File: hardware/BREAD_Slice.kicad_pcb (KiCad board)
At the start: 2 copper layers, 70 x 100 mm, 16 parts, among them J1 Conn_01x10_Female, U1 AP63205

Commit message: initial commit, complete schematic and board
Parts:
- added C10: 0.1u, Capacitor_SMD:C_0805_2012Metric_Pad1.18x1.45mm_HandSolder, F.Cu at (172.6, 102.2)
- added C11: 0.1u, Capacitor_SMD:C_0805_2012Metric_Pad1.18x1.45mm_HandSolder, F.Cu at (170.4, 65.9)
- added C12: 0.1u, Capacitor_SMD:C_0805_2012Metric_Pad1.18x1.45mm_HandSolder, F.Cu at (172.5, 65.9)
- added C5: 0.1u, Capacitor_SMD:C_0805_2012Metric_Pad1.18x1.45mm_HandSolder, F.Cu at (170.4, 120.5)
- added C6: 0.1u, Capacitor_SMD:C_0805_2012Metric_Pad1.18x1.45mm_HandSolder, F.Cu at (172.6, 120.5)
- added C7: 0.1u, Capacitor_SMD:C_0805_2012Metric_Pad1.18x1.45mm_HandSolder, F.Cu at (170.5, 84.1)
- added C8: 0.1u, Capacitor_SMD:C_0805_2012Metric_Pad1.18x1.45mm_HandSolder, F.Cu at (172.6, 84.1)
- added C9: 0.1u, Capacitor_SMD:C_0805_2012Metric_Pad1.18x1.45mm_HandSolder, F.Cu at (170.4, 102.2)
- added Cl1: 100n, Capacitor_SMD:C_0805_2012Metric_Pad1.18x1.45mm_HandSolder, F.Cu at (179.8, 112.9)
- added Cl2: 100n, Capacitor_SMD:C_0805_2012Metric_Pad1.18x1.45mm_HandSolder, F.Cu at (179.8, 76.5)
- added Cl3: 100n, Capacitor_SMD:C_0805_2012Metric_Pad1.18x1.45mm_HandSolder, F.Cu at (179.8, 94.5)
- added Cl4: 100n, Capacitor_SMD:C_0805_2012Metric_Pad1.18x1.45mm_HandSolder, F.Cu at (179.7, 58.3)
- added FB1: FerriteBead, Resistor_SMD:R_0805_2012Metric_Pad1.20x1.40mm_HandSolder, F.Cu at (174.6, 120.5)
- added FB2: FerriteBead, Resistor_SMD:R_0805_2012Metric_Pad1.20x1.40mm_HandSolder, F.Cu at (174.7, 84.1)
- added FB3: FerriteBead, Resistor_SMD:R_0805_2012Metric_Pad1.20x1.40mm_HandSolder, F.Cu at (174.7, 102.2)
- added FB4: FerriteBead, Resistor_SMD:R_0805_2012Metric_Pad1.20x1.40mm_HandSolder, F.Cu at (174.6, 65.9)
- added J2: Screw_Terminal_01x02, TerminalBlock_4Ucon:TerminalBlock_4Ucon_1x02_P3.50mm_Horizontal, F.Cu at (187.7, 118.0)
- added J3: Screw_Terminal_01x02, TerminalBlock_4Ucon:TerminalBlock_4Ucon_1x02_P3.50mm_Horizontal, F.Cu at (187.7, 109.0)
- added J4: Screw_Terminal_01x02, TerminalBlock_4Ucon:TerminalBlock_4Ucon_1x02_P3.50mm_Horizontal, F.Cu at (187.7, 99.7)
- added J5: Screw_Terminal_01x02, TerminalBlock_4Ucon:TerminalBlock_4Ucon_1x02_P3.50mm_Horizontal, F.Cu at (187.7, 90.6)
- added J6: Screw_Terminal_01x02, TerminalBlock_4Ucon:TerminalBlock_4Ucon_1x02_P3.50mm_Horizontal, F.Cu at (187.8, 81.5)
- added J7: Screw_Terminal_01x02, TerminalBlock_4Ucon:TerminalBlock_4Ucon_1x02_P3.50mm_Horizontal, F.Cu at (187.7, 72.5)
- added J8: Screw_Terminal_01x02, TerminalBlock_4Ucon:TerminalBlock_4Ucon_1x02_P3.50mm_Horizontal, F.Cu at (187.7, 63.4)
- added J9: Screw_Terminal_01x02, TerminalBlock_4Ucon:TerminalBlock_4Ucon_1x02_P3.50mm_Horizontal, F.Cu at (187.7, 54.3)
- added JP1: JUMP1, Jumper:SolderJumper-2_P1.3mm_Open_TrianglePad1.0x1.5mm, F.Cu at (179.4, 120.3)
- added JP10: JUMP2, Jumper:SolderJumper-2_P1.3mm_Bridged_RoundedPad1.0x1.5mm, F.Cu at (180.4, 98.8)
- added JP11: JUMP3, Jumper:SolderJumper-2_P1.3mm_Open_TrianglePad1.0x1.5mm, F.Cu at (182.1, 102.0)
- added JP12: JUMP4, Jumper:SolderJumper-2_P1.3mm_Open_TrianglePad1.0x1.5mm, F.Cu at (182.2, 92.0)
- added JP13: JUMP1, Jumper:SolderJumper-2_P1.3mm_Open_TrianglePad1.0x1.5mm, F.Cu at (179.4, 65.7)
- added JP14: JUMP2, Jumper:SolderJumper-2_P1.3mm_Bridged_RoundedPad1.0x1.5mm, F.Cu at (180.3, 62.5)
- added JP15: JUMP3, Jumper:SolderJumper-2_P1.3mm_Open_TrianglePad1.0x1.5mm, F.Cu at (182.1, 65.7)
- added JP16: JUMP4, Jumper:SolderJumper-2_P1.3mm_Open_TrianglePad1.0x1.5mm, F.Cu at (182.1, 55.8)
- added JP2: JUMP2, Jumper:SolderJumper-2_P1.3mm_Bridged_RoundedPad1.0x1.5mm, F.Cu at (180.4, 117.1)
- added JP3: JUMP3, Jumper:SolderJumper-2_P1.3mm_Open_TrianglePad1.0x1.5mm, F.Cu at (182.1, 120.3)
- added JP4: JUMP4, Jumper:SolderJumper-2_P1.3mm_Open_TrianglePad1.0x1.5mm, F.Cu at (182.1, 110.4)
- added JP5: JUMP1, Jumper:SolderJumper-2_P1.3mm_Open_TrianglePad1.0x1.5mm, F.Cu at (179.4, 83.9)
- added JP6: JUMP2, Jumper:SolderJumper-2_P1.3mm_Bridged_RoundedPad1.0x1.5mm, F.Cu at (180.4, 80.7)
- added JP7: JUMP3, Jumper:SolderJumper-2_P1.3mm_Open_TrianglePad1.0x1.5mm, F.Cu at (182.1, 83.9)
- added JP8: JUMP4, Jumper:SolderJumper-2_P1.3mm_Open_TrianglePad1.0x1.5mm, F.Cu at (182.2, 74.0)
- added JP9: JUMP1, Jumper:SolderJumper-2_P1.3mm_Open_TrianglePad1.0x1.5mm, F.Cu at (179.4, 102.0)
- added R1: 10k, Resistor_SMD:R_0805_2012Metric_Pad1.20x1.40mm_HandSolder, F.Cu at (157.4, 91.7)
- added Rref1: 430R / 4300R 0.1%, Resistor_SMD:R_0805_2012Metric_Pad1.20x1.40mm_HandSolder, F.Cu at (176.9, 121.0)
- added Rref2: 430R / 4300R 0.1%, Resistor_SMD:R_0805_2012Metric_Pad1.20x1.40mm_HandSolder, F.Cu at (176.9, 84.5)
- added Rref3: 430R / 4300R 0.1%, Resistor_SMD:R_0805_2012Metric_Pad1.20x1.40mm_HandSolder, F.Cu at (176.9, 102.7)
- added Rref4: 430R / 4300R 0.1%, Resistor_SMD:R_0805_2012Metric_Pad1.20x1.40mm_HandSolder, F.Cu at (176.9, 66.4)
- added U2: TXB0108PW, Package_SO:TSSOP-20_4.4x6.5mm_P0.65mm, F.Cu at (159.3, 87.1)
- added U3: MAX31865xAP, Package_SO:SSOP-20_5.3x7.2mm_P0.65mm, F.Cu at (174.7, 113.6)
- added U4: MAX31865xAP, Package_SO:SSOP-20_5.3x7.2mm_P0.65mm, F.Cu at (174.8, 77.2)
- added U5: MAX31865xAP, Package_SO:SSOP-20_5.3x7.2mm_P0.65mm, F.Cu at (174.8, 95.3)
- added U6: MAX31865xAP, Package_SO:SSOP-20_5.3x7.2mm_P0.65mm, F.Cu at (174.7, 59.0)
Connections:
- A1 pad 10: unconnected-(A1-D7-Pad10) -> /CS4
- A1 pad 11: unconnected-(A1-D8-Pad11) -> /CS3
- A1 pad 12: unconnected-(A1-D9-Pad12) -> /CS2
- A1 pad 13: unconnected-(A1-D10-Pad13) -> /CS1
- A1 pad 14: unconnected-(A1-D11-Pad14) -> /MOSI
- A1 pad 15: unconnected-(A1-D12-Pad15) -> /MISO
- A1 pad 16: unconnected-(A1-D13-Pad16) -> /SCK
- A1 pad 17: unconnected-(A1-3V3-Pad17) -> +3.3V
- A1 pad 19: unconnected-(A1-A0-Pad19) -> /DRDY1
- A1 pad 20: unconnected-(A1-A1-Pad20) -> /DRDY2
- A1 pad 21: unconnected-(A1-A2-Pad21) -> /DRDY4
- A1 pad 22: unconnected-(A1-A3-Pad22) -> /DRDY3
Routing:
- net +3.3V: track 0.00 -> 125.6 mm, vias 0 -> 6
- net /SCK_3V: track 0.00 -> 117.2 mm
- net /MISO_3V: track 0.00 -> 99.8 mm, vias 0 -> 2
- net /MOSI_3V: track 0.00 -> 98.8 mm, vias 0 -> 2
- net /DRDY4: track 0.00 -> 70.6 mm, vias 0 -> 2
- net /DRDY3: track 0.00 -> 53.2 mm, vias 0 -> 2
- net /SCK: track 0.00 -> 50.8 mm
- net /MISO: track 0.00 -> 50.4 mm
- net GND: track 16.8 -> 67.0 mm, vias 20 -> 380
- net /MOSI: track 0.00 -> 48.5 mm
- net /CS1: track 0.00 -> 46.6 mm
- net /CS2: track 0.00 -> 44.7 mm
- net /CS3: track 0.00 -> 42.8 mm
- net /CS4: track 0.00 -> 40.9 mm
- net /CS1_3V: track 0.00 -> 37.9 mm, vias 0 -> 2
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- added copper zone on F.Cu, net GND
- removed copper zone on B.Cu, net GNDPWR
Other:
- board text added: "BREAD Slice RTD Measurement SLC_RTDM R3 04-2025"
- board text added: "JUMP1"
- board text added: "JUMP2"
- board text added: "JUMP3"
- board text added: "JUMP4"
- board text removed: "BREAD Slice Template SLC_TEMP R3 04-2025"

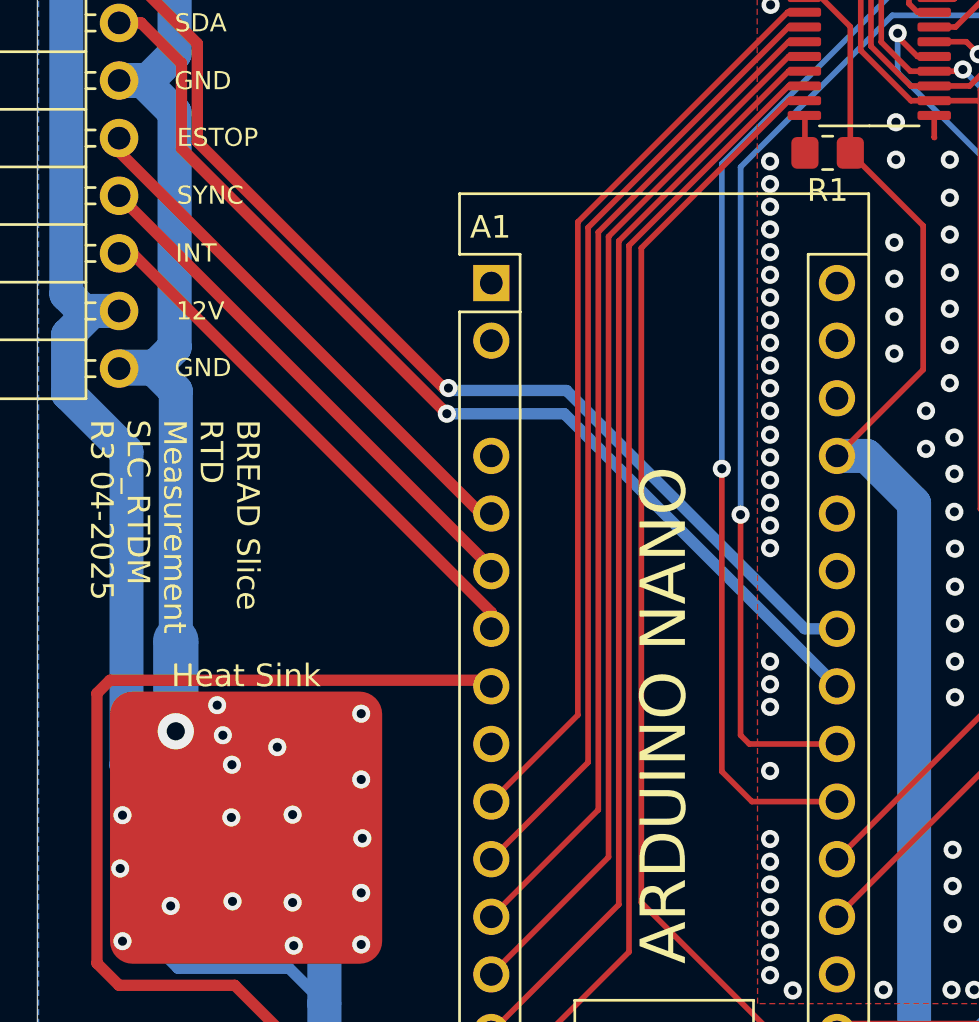
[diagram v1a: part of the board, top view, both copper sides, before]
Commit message: review and revise board to use kmlib properly and clear drc/erc
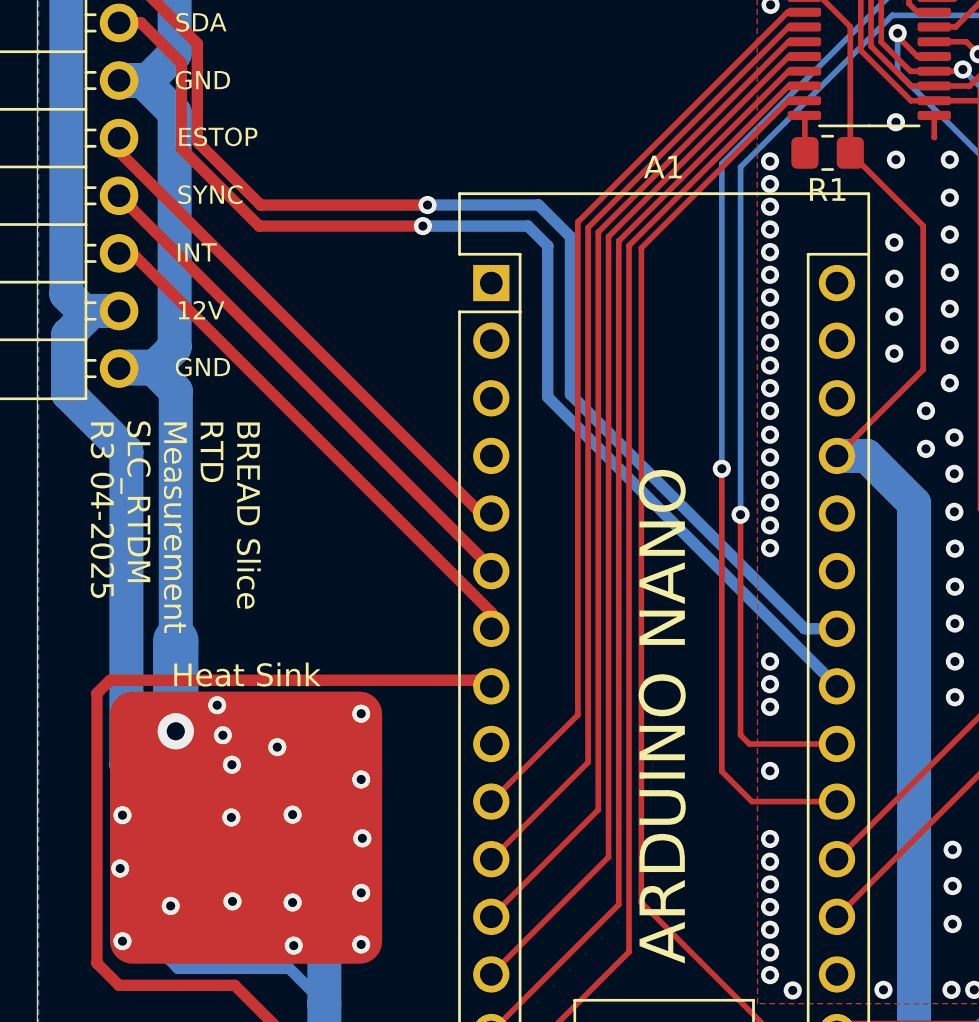
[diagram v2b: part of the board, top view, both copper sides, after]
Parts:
- A1: footprint Module:Arduino_Nano -> KMLib_Boards_Modules:Arduino_Nano_Headers
- D1: footprint SparkFun-LED:WS2812-5050-4PIN -> KMLib_IC_SMD:WS2812-5050-4PIN
- HS1: footprint kml-custom:Thermal Pad -> KMLib_Mounting:Thermal Pad
- U1: footprint Package_TO_SOT_SMD:TSOT-23-6 -> KMLib_IC_SMD:SOIC_05WU-7_DIO
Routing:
- net /I2C_CLK: track 46.3 -> 50.4 mm
- net /I2C_DAT: track 46.0 -> 49.9 mm
